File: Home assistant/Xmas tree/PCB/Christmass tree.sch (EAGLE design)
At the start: 12 parts, among them T1 BC547, X1 3PIN_5MM_TERMINAL

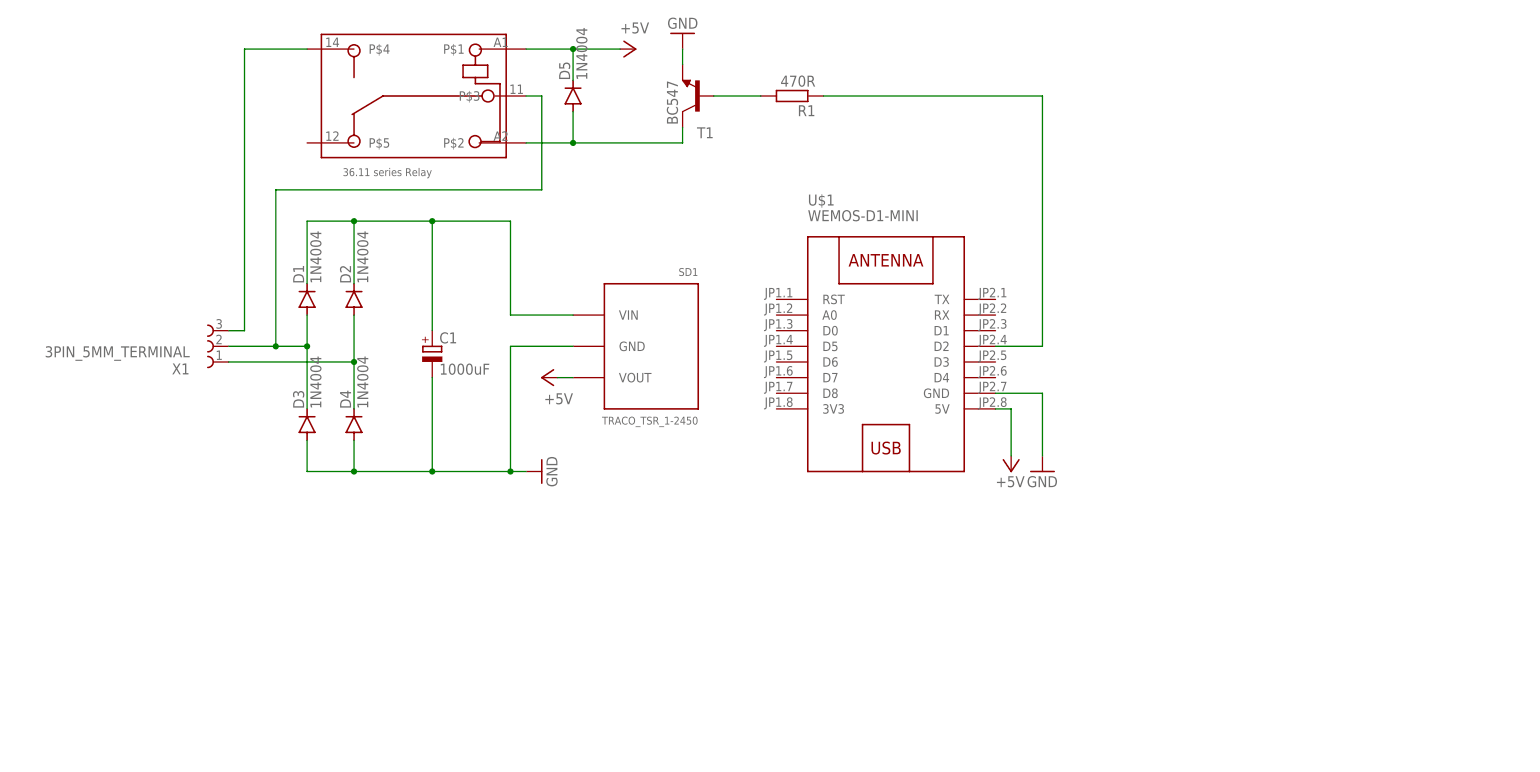
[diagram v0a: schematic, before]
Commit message: Triac christmass tree
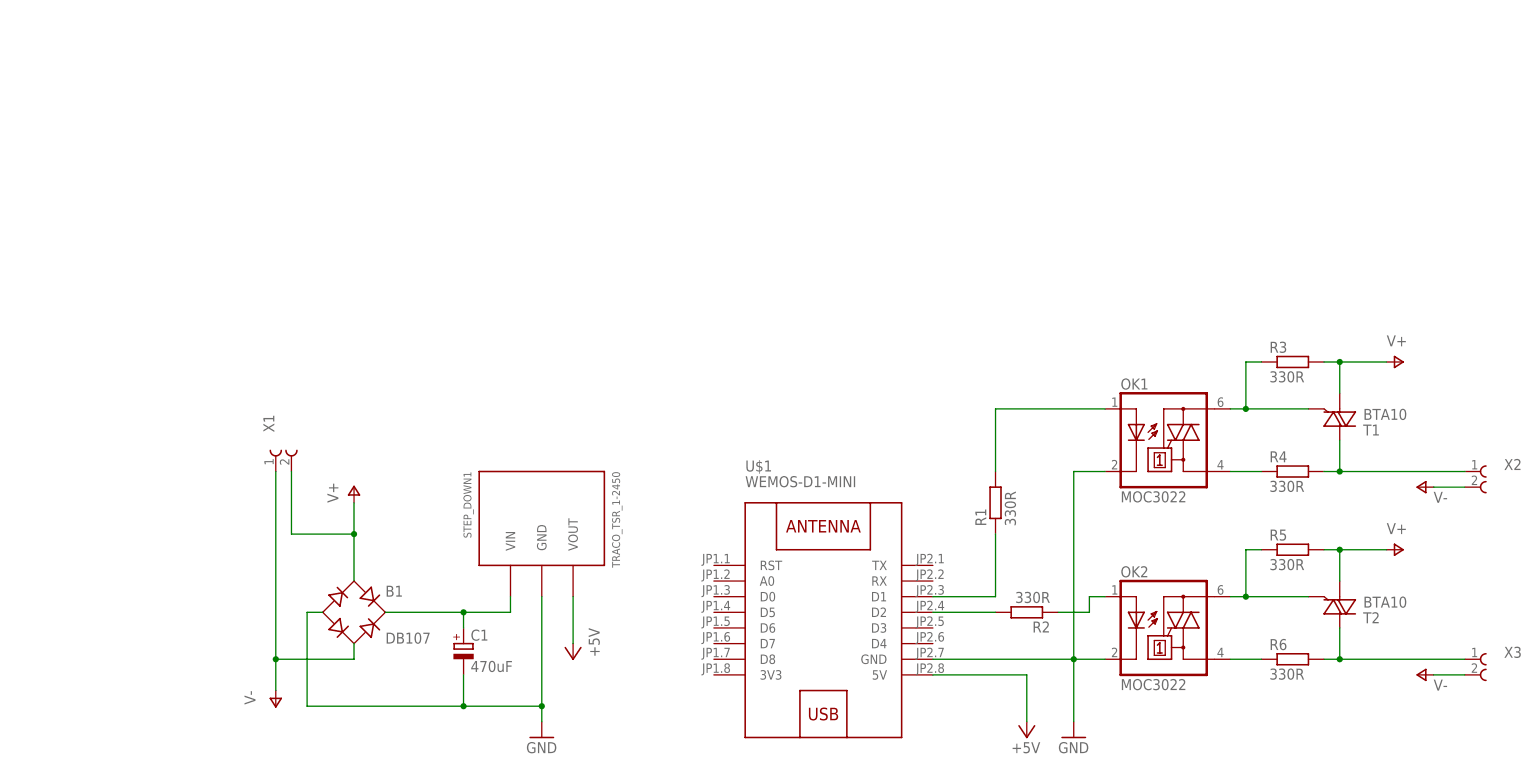
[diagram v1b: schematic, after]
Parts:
- removed D1, D2, D3, D4, D5: 1N4004, diode:1N4004
- removed RL1: 36.11, Rele_Finder:36.11
- removed SD1: TRACO_TSR_1-2450, Voltage:TRACO_TSR_1-2450
- added B1: DB107, rectifier:DBDB107G
- added OK1, OK2: MOC3022, optocoupler:MOC3031M
- added R2, R3, R4, R5, R6: 330R, resistor:R-EU_0204/7
- added STEP_DOWN1: TRACO_TSR_1-2450, Voltage:TRACO_TSR_1-2450
- added T2: BTA10, triac:TIC253
- added X2, X3: 2PIN_5MM_TERMINAL, Terminaly:2PIN_5MM_TERMINAL
- C1: value 1000uF -> 470uF; device resistor:CPOL-EUE3.5-10 -> resistor:CPOL-EUE5-10.5
- R1: value 470R -> 330R; device resistor:R-EU_0207/10 -> resistor:R-EU_0204/7
- T1: value BC547 -> BTA10; device transistor:BC547-NPN-TO92-CBE -> triac:TIC253
- U$1: device Sbirka modulu:WEMOS-D1-MINI -> Sbirka modulu:WEMOS-D1-MINIBEZ_POTISKU
- X1: value 3PIN_5MM_TERMINAL -> 2PIN_5MM_TERMINAL; device Terminaly:3PIN_5MM_TERMINAL -> Terminaly:2PIN_5MM_TERMINAL
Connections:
- removed net +12VAC: D1.A, D3.C, RL1.P$3, X1.2
- removed net -12VAC: D2.A, D4.C, X1.1
- removed net 12VDC: C1.+, D1.C, D2.C, SD1.VIN
- removed net OUTPUT: RL1.P$4, X1.3
- new net N$10: R4.2, T1.A2, X2.1
- new net N$13: OK2.A1, R6.1
- new net N$14: R6.2, T2.A2, X3.1
- new net N$2: OK2.A, R2.1
- new net N$3: B1.+, C1.+, STEP_DOWN1.VIN
- new net N$7: OK1.A2, R3.1, T1.G
- new net N$8: OK2.A2, R5.1, T2.G
- new net N$9: OK1.A1, R4.1
- new net V+: B1.AC1, R3.2, R5.2, T1.A1, T2.A1, X1.2
- new net V-: B1.AC2, X1.1, X2.2, X3.2
- net +5V: now also STEP_DOWN1.VOUT; no longer D5.C, RL1.P$1, SD1.VOUT
- net GND: now also B1.-, OK1.C, OK2.C, STEP_DOWN1.GND; no longer D3.A, D4.A, SD1.GND, T1.E
- net N$4: now also R2.2, U$1.D2; no longer R1.2, T1.B
- net N$5: now also R1.1, U$1.D1; no longer D5.A, RL1.P$2, T1.C
- net N$6: now also OK1.A, R1.2; no longer R1.1, U$1.D2
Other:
- moved on the sheet: C1, R1, U$1
